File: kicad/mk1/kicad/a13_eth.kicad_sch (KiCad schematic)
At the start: 46 parts, among them J4 ARJM11, J8 Conn_1x06, U13 TPD4EUSB30, U24 93LCxxA, U7 LAN9512, Y5 25Mhz

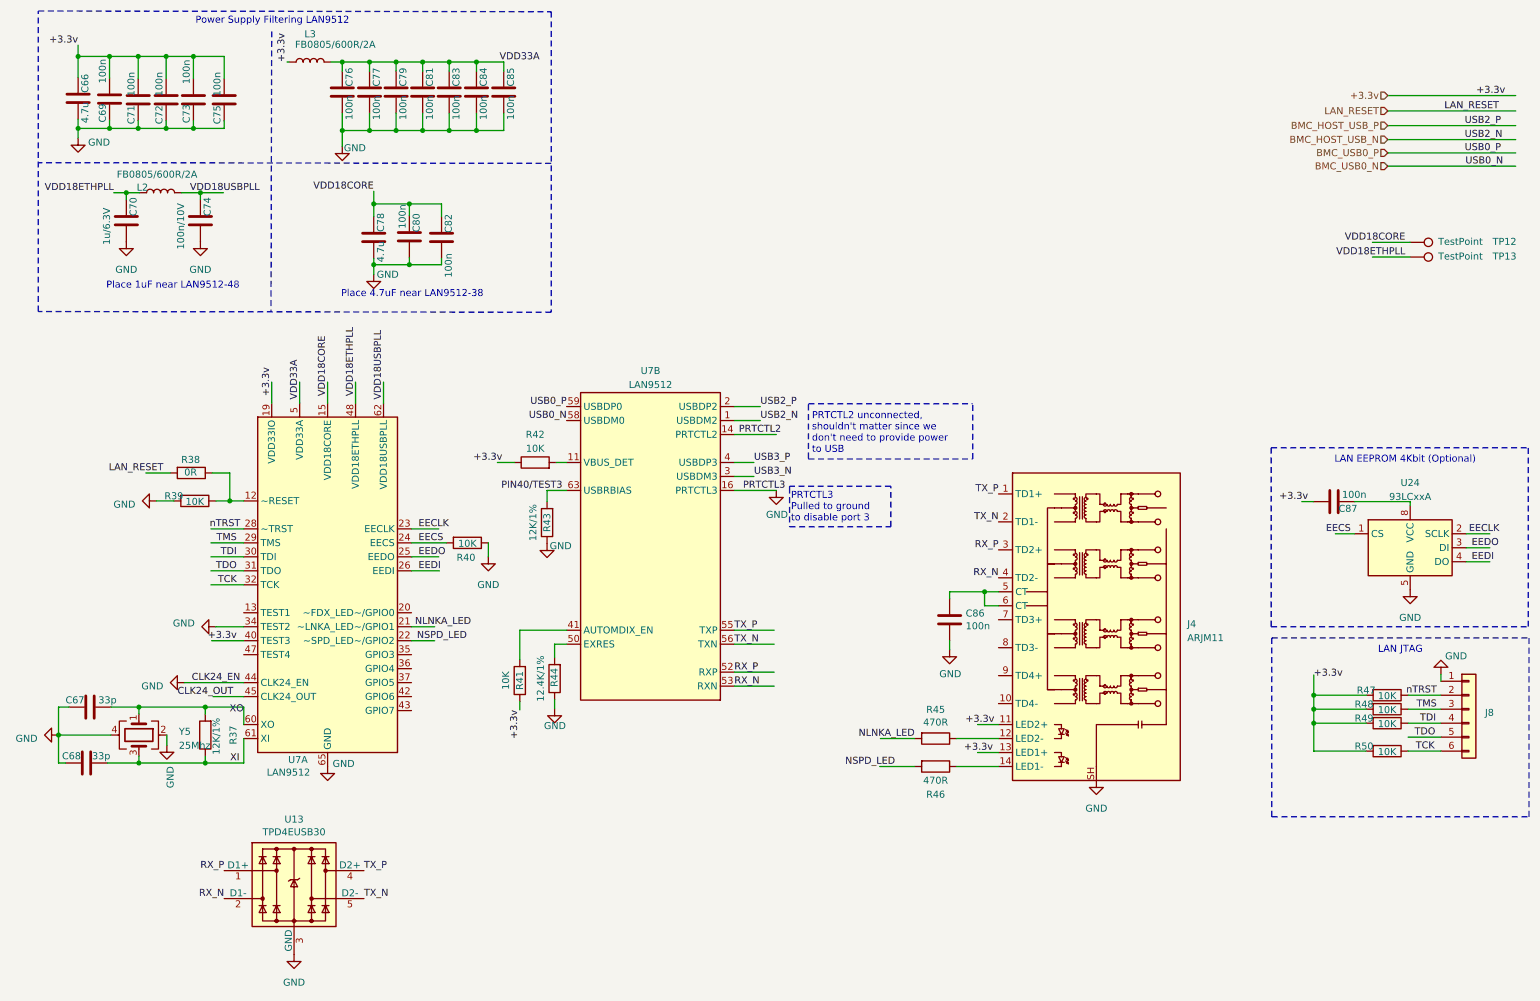
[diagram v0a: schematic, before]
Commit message: work on schematics
* add power rail
* import CM4 related part
* design most of the BMC-PHY part
* create new library/footprint for rp t113-s3 SOM
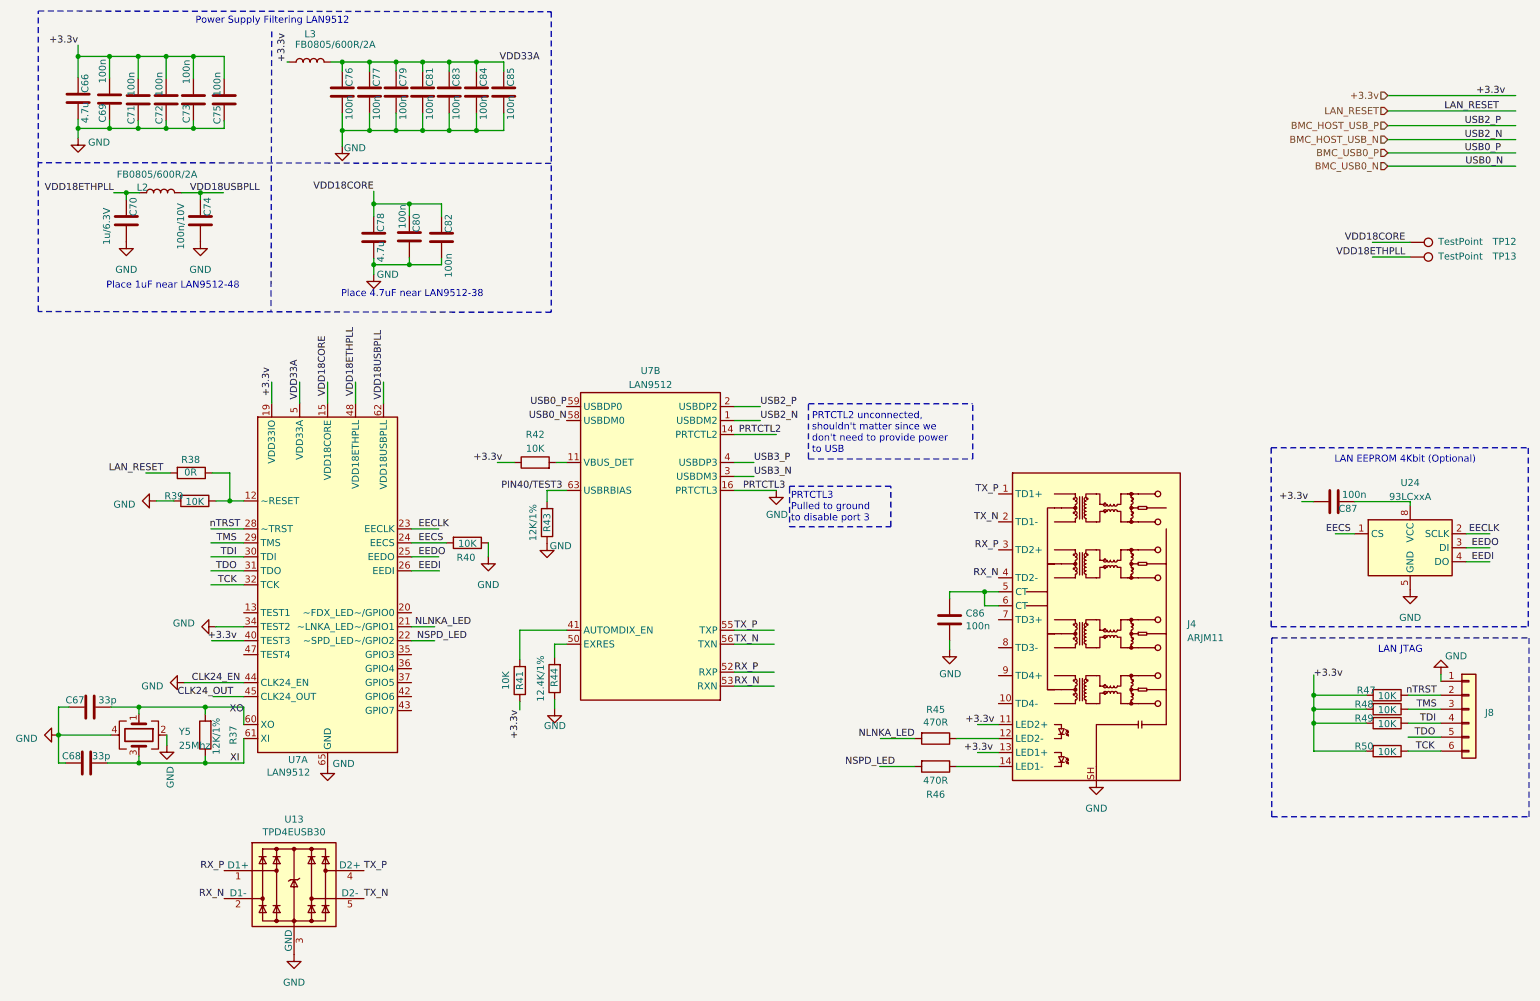
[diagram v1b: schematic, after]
